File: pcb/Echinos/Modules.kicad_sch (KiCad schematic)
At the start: 12 parts, among them J209 Joystick, J4 FPC (module), U205 PMW3360DM-T2QU, U206 VRH1902LTX

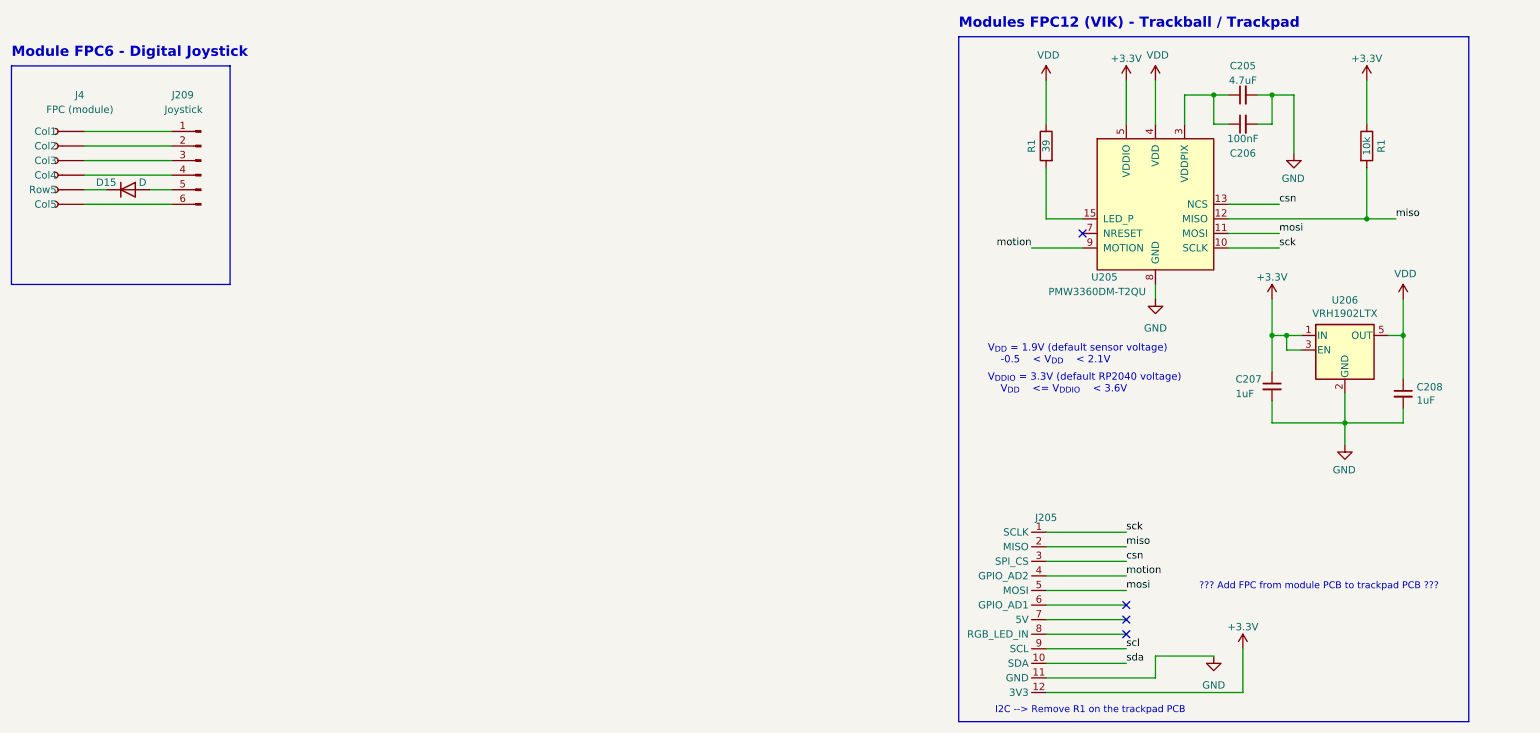
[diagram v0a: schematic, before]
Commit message: 🚧 [PCB] - Backup before trying to add 5.0V support.
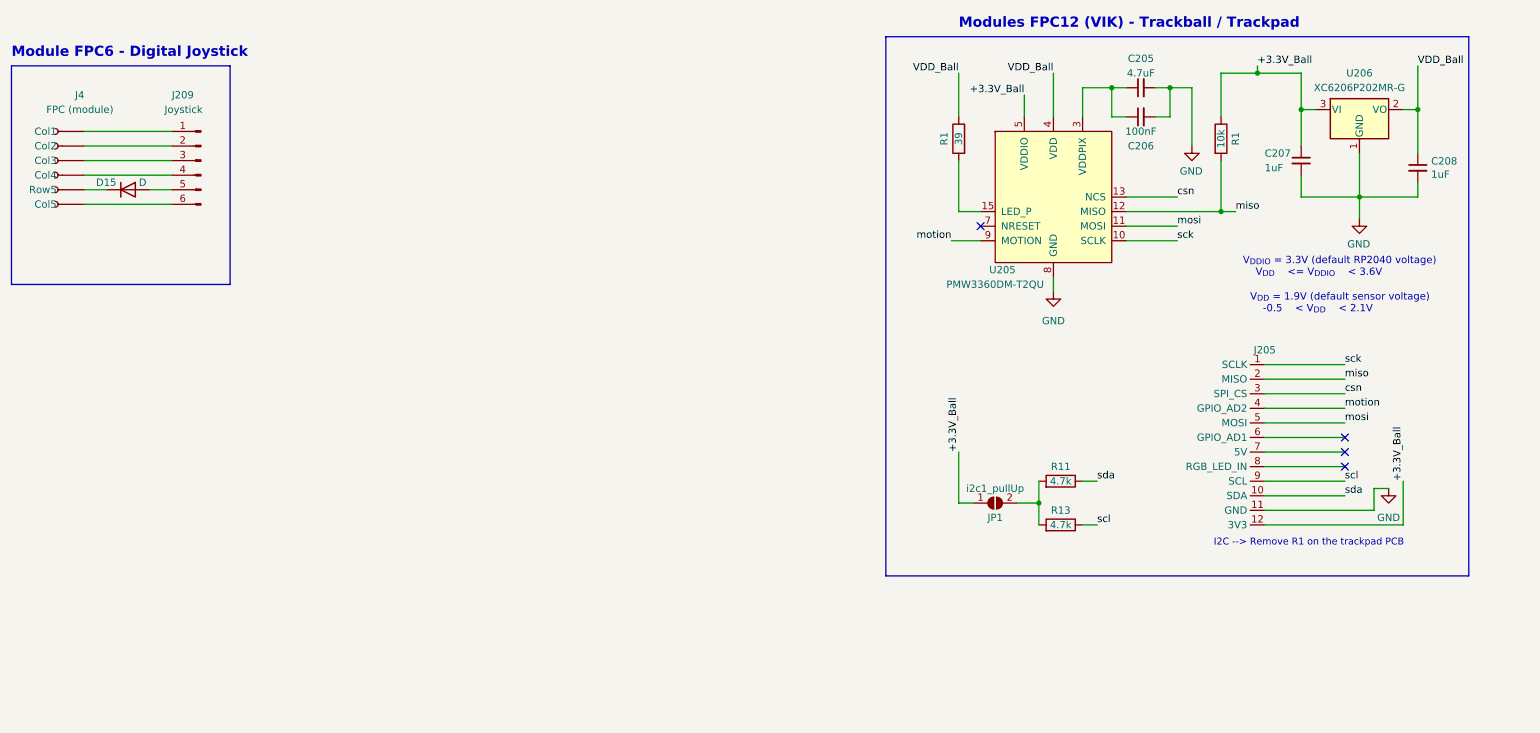
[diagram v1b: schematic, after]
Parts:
- added JP1: i2c1_pullUp, Echinos:SolderJumper_Open_0.8x1.2mm, symbol Jumper:SolderJumper_2_Open
- added R11, R13: 4.7k, Resistor_SMD:R_0402_1005Metric_Pad0.72x0.64mm_HandSolder, symbol Device:R
- U206: value VRH1902LTX -> XC6206P202MR-G; footprint Package_TO_SOT_SMD:SOT-23-5_HandSoldering -> Package_TO_SOT_SMD:SOT-23-3; symbol Regulator_Linear:TLV70019_SOT23-5 -> Regulator_Linear:XC6206PxxxMR; JLCPCB Rotation Offset -90 -> 0; LCSC C697975 -> C2891260
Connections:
- net GND: now also U206.1 (GND); no longer U206.2 (GND)
- net scl: now also R13.1
- net sda: now also R11.1
- net +3.3V renamed +3.3V_Ball
- net +3.3V_Ball: now also JP1.1 (A); no longer U206.1 (IN)
- net VDD renamed VDD_Ball
- net VDD_Ball: now also U206.2 (VO); no longer U206.5 (OUT)
- new net: JP1.2 (B), R11.2, R13.2
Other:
- note removed: "??? Add FPC from module PCB to trackpad PCB ???"
- moved on the sheet: C205, C206, C207, C208, J205, R1, U205

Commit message: [PCB] - Save last state with in-board MCU.
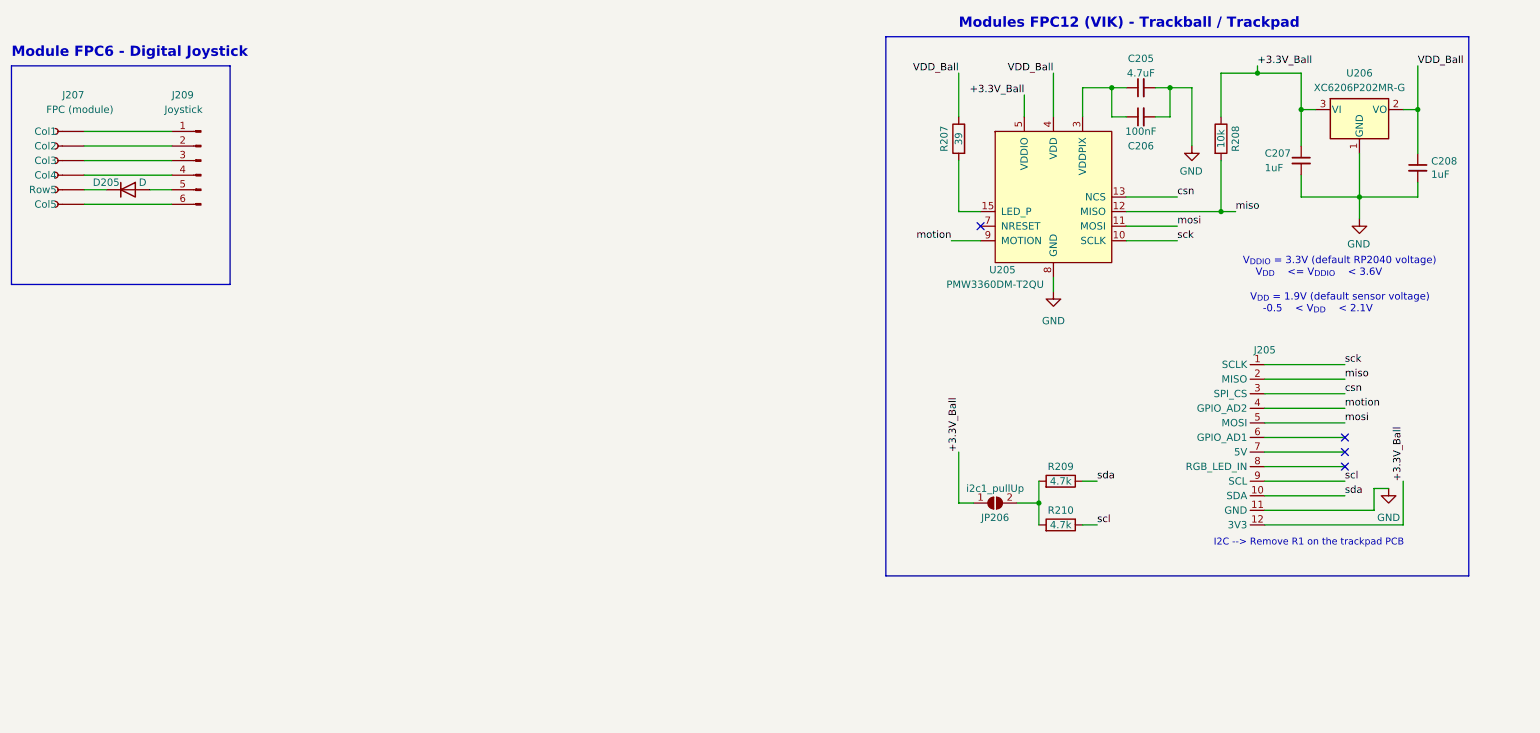
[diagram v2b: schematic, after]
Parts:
- U206: value XC6206P202MR-G -> XC6206P202MR-G
- renumbered D15 to D205, J4 to J207, JP1 to JP206, R1 to R207, R1 to R208, R11 to R209, R13 to R210

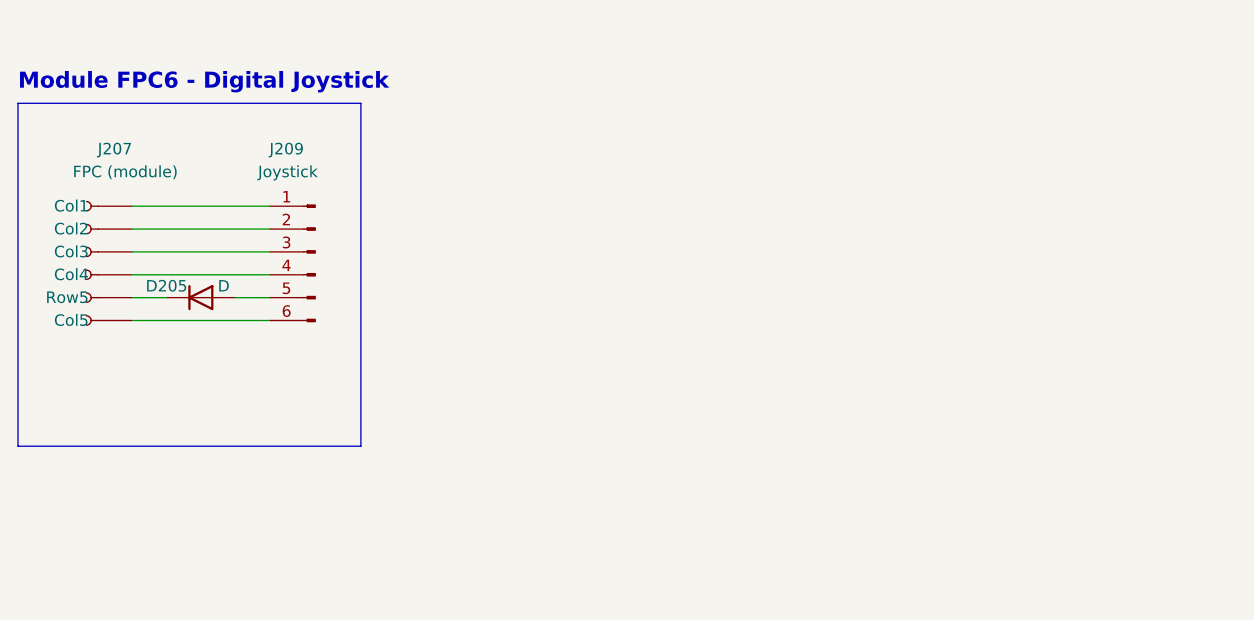
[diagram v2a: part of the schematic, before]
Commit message: [PCB] - Save last state with Helios MCU board and gasket tabs on PCB.
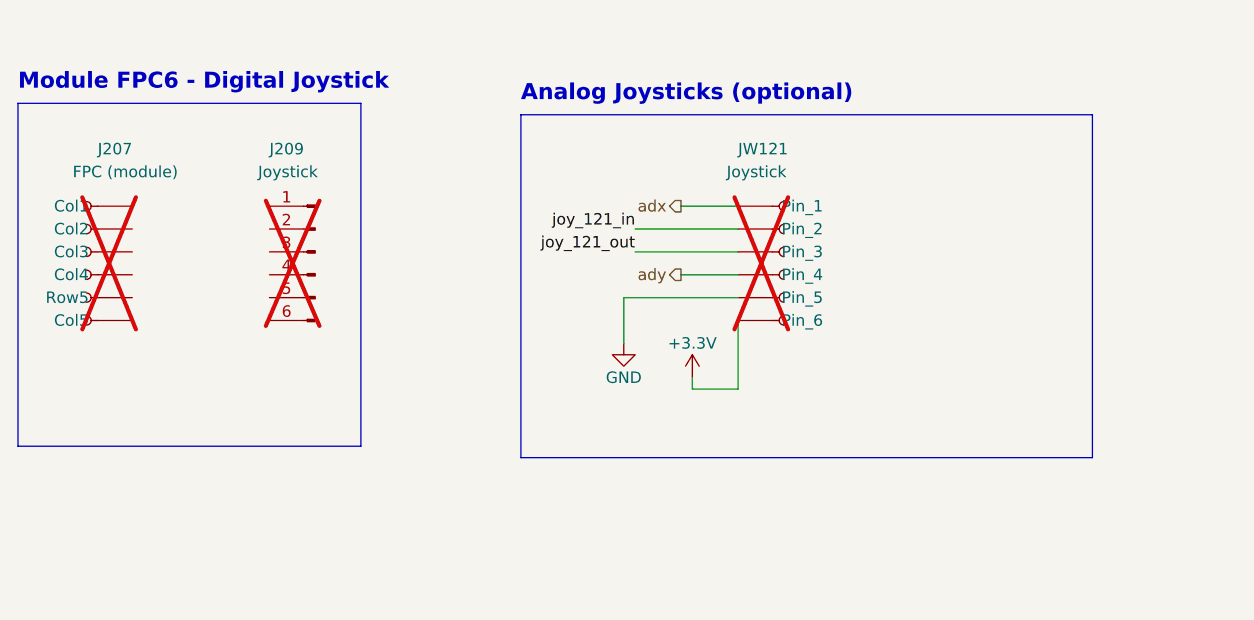
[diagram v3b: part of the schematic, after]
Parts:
- removed D205: D, Echinos:D_SOD123, symbol Device:D
- added JW121: Joystick, Echinos:Joystick_KSilver_JP19, symbol Connector:Conn_01x06_Socket
- J207, J209: now not fitted; now left out of the parts list
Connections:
- net GND: now also JW121.5 (Pin_5)
- net at J209.1 (Pin_1): no longer J207.1 (Pin_1)
- net at J209.2 (Pin_2): no longer J207.2 (Pin_2)
- net at J209.3 (Pin_3): no longer J207.3 (Pin_3)
- net at J209.4 (Pin_4): no longer J207.4 (Pin_4)
- net at J209.6 (Pin_6): no longer J207.6 (Pin_6)
- new net +3.3V: JW121.6 (Pin_6)
- new net adx: JW121.1 (Pin_1)
- new net ady: JW121.4 (Pin_4)
- new net joy_121_in: JW121.2 (Pin_2)
- new net joy_121_out: JW121.3 (Pin_3)
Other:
- note added: "Analog Joysticks (optional)"

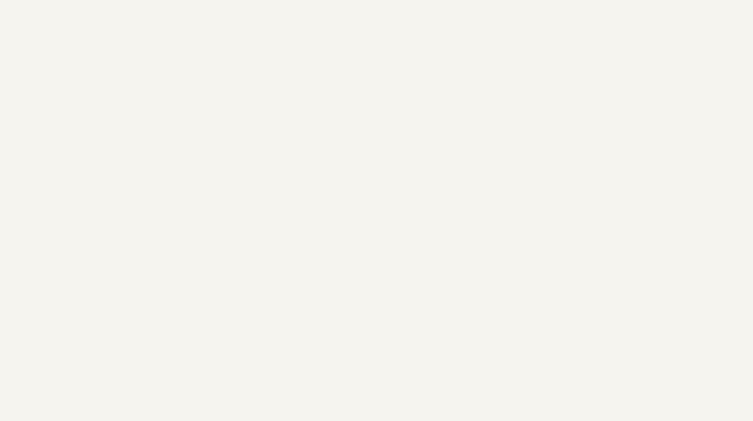
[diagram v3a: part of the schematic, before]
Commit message: [PCB] - Save last state with on board RP2040.   - Clean schematics   - Fix flash capacitor value   - Fix flash schema to match all footprint pins   - Pass ERC (schema and pcb)   - Select missing LCSC components (USBC/B, buttons, vik connector)   - Add more margin to lateral pads in USB B footprint   - Improve top plane grounding under switches   - Adjust orientation and position to match JLCPCB   - Clean unused fields in schematics   - Add VIK connector footprint to lib (updated to match more models)   - Harmonization of footprints packaging for caps and resistors (either 0805 or 0402)   - Check availability and correctness of all parts   - Fix space in fields (was LCSC2 on leds)
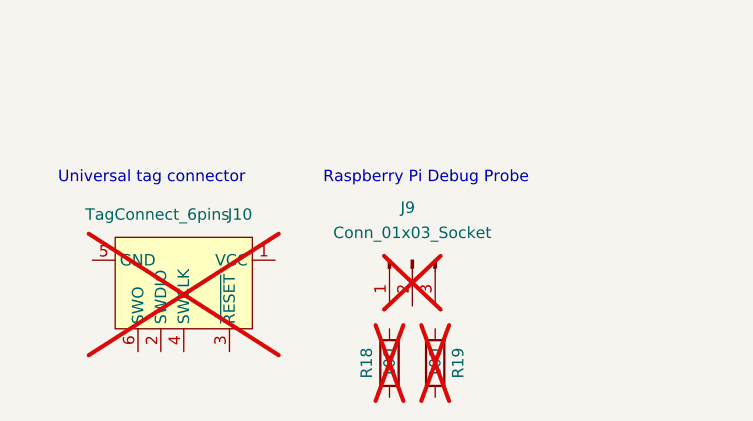
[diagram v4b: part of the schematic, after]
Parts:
- added J10: TagConnect_6pins, Connector:Tag-Connect_TC2030-IDC-FP_2x03_P1.27mm_Vertical, symbol Connector:Conn_ARM_SWD_TagConnect_TC2030
- added J9: Conn_01x03_Socket, Connector_JST:JST_SH_BM03B-SRSS-TB_1x03-1MP_P1.00mm_Vertical, symbol Connector:Conn_01x03_Pin
- added R18, R19: 100, Resistor_SMD:R_0805_2012Metric, symbol Device:R
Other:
- note added: "Raspberry Pi Debug Probe"
- note added: "Universal tag connector"
